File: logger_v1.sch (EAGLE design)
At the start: 141 parts, among them IC1 74HC595N, IC10 DS1307, IC12 LTC485N, IC2 7805T, IC4 REG1117, IC5 25LC080P, IC7 ATMEGA168-20P, IC9 LM358N, Q3 FQN1N50CI, Q4 32.768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

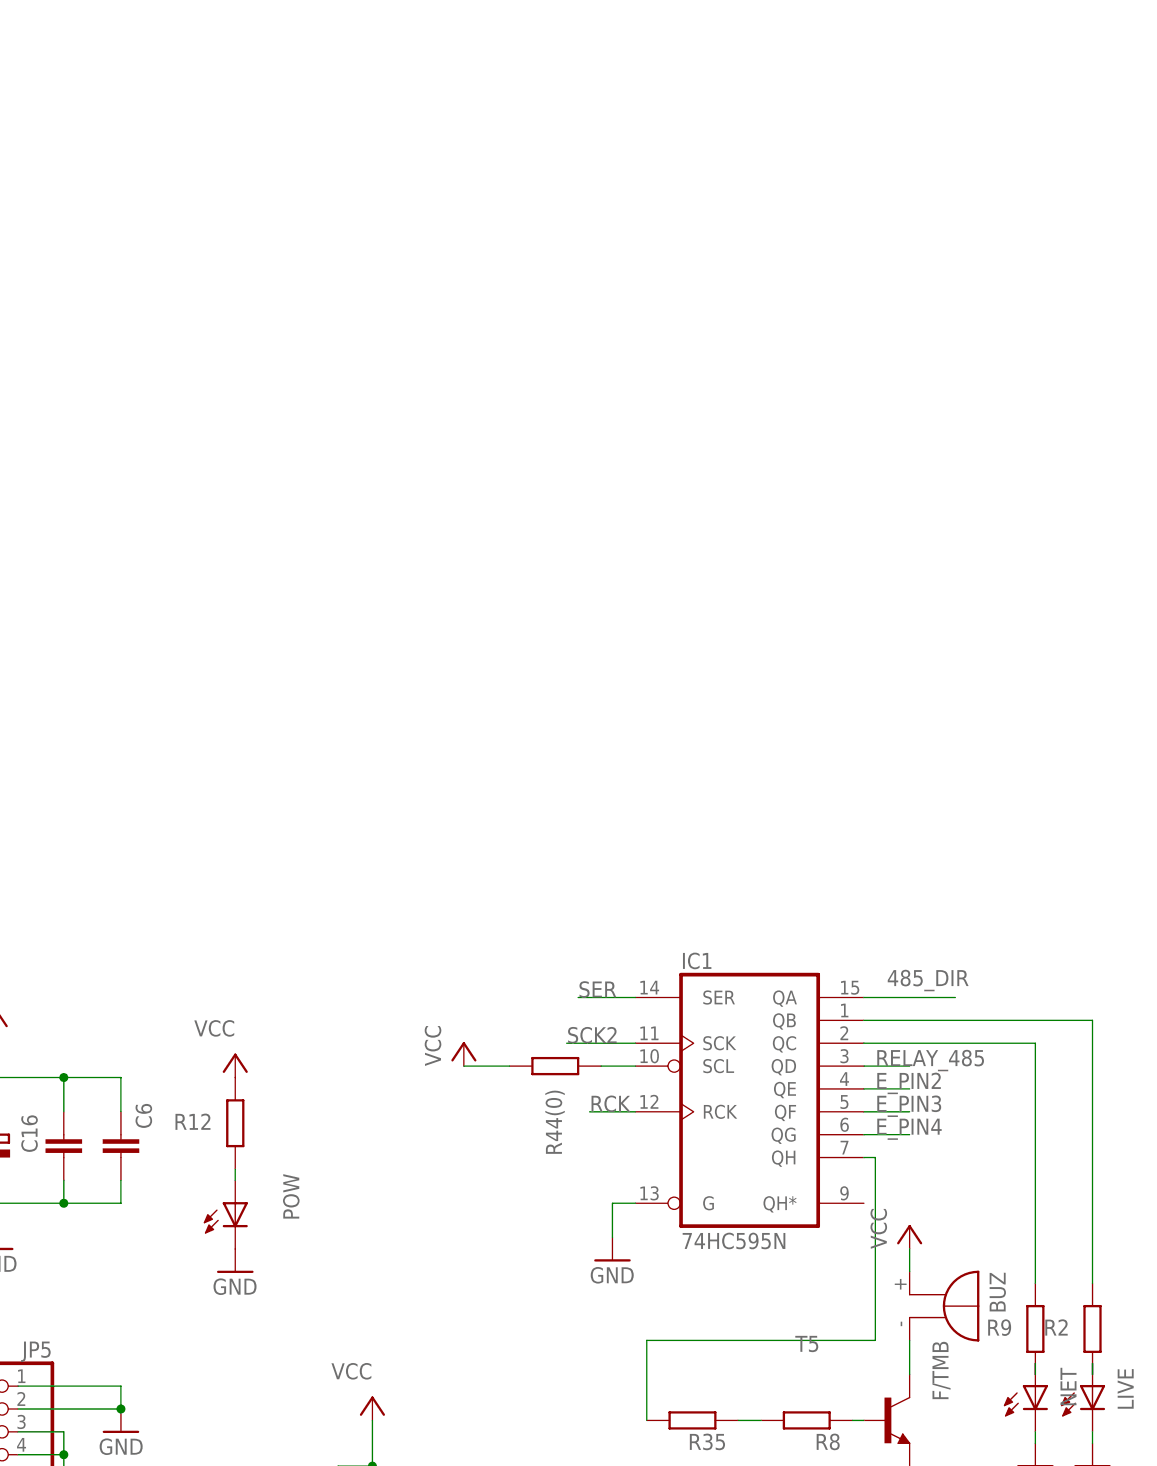
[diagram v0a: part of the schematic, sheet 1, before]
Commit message: led button ckt added
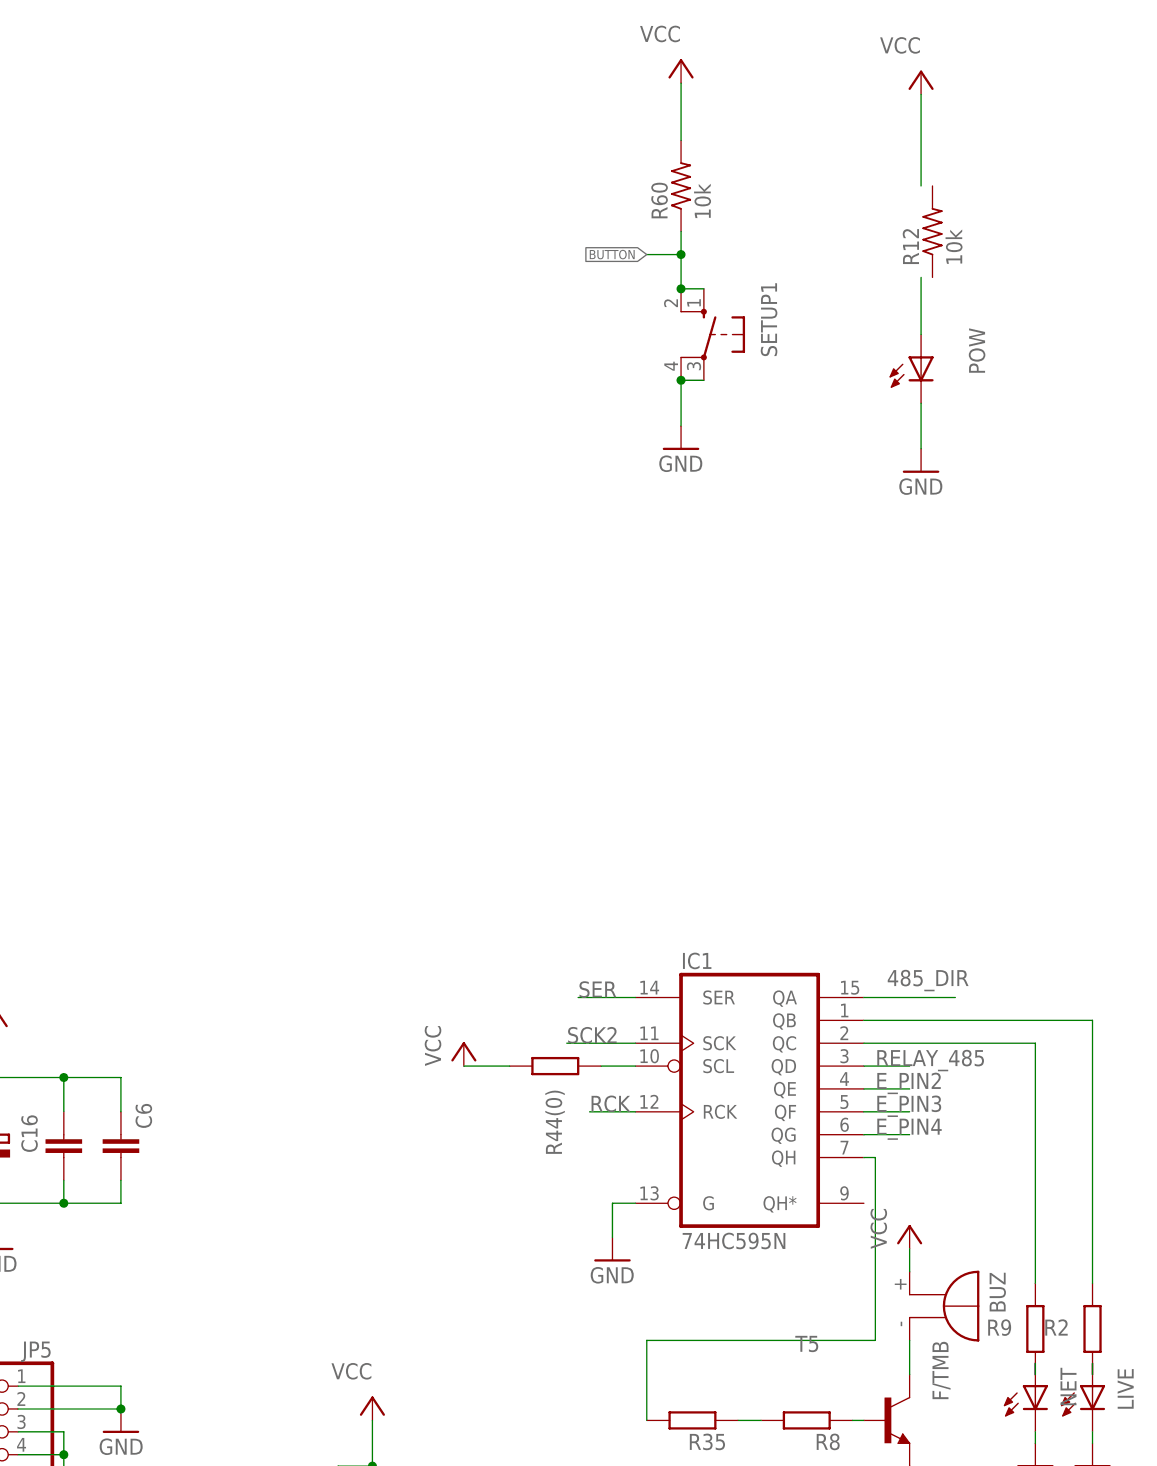
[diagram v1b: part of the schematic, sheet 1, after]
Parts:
- added R60: 10k, resistor:R-US_R0805
- added SETUP1: (no value), switch-omron:10-XX
- R12: value (none) -> 10k; device rcl:R-EU_0204/7 -> resistor:R-US_R0805
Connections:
- new net BUTTON: R60.1, SETUP1.S, SETUP1.S1
- net GND: now also SETUP1.P, SETUP1.P1
- net N$30: no longer R12.1
- net VCC: now also R60.2; no longer R12.2
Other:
- moved on the sheet: POW
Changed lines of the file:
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@@
 <setting verticaltext="up"/>
 </settings>
-<grid distance="0.05" unitdist="inch" unit="inch" style="lines" multiple="1" display="no" altdistance="0.01" altunitdist="inch" altunit="inch"/>
+<grid distance="0.1" unitdist="inch" unit="inch" style="lines" multiple="1" display="no" altdistance="0.01" altunitdist="inch" altunit="inch"/>
 <layers>
 <layer number="1" name="Top" color="4" fill="1" visible="no" active="no"/>
@@
 <layer number="59" name="tCarbon" color="7" fill="1" visible="no" active="no"/>
 <layer number="60" name="bCarbon" color="7" fill="1" visible="no" active="no"/>
+<layer number="88" name="SimResults" color="9" fill="1" visible="no" active="yes"/>
+<layer number="89" name="SimProbes" color="9" fill="1" visible="no" active="yes"/>
 <layer number="90" name="Modules" color="5" fill="1" visible="yes" active="yes"/>
 <layer number="91" name="Nets" color="2" fill="1" visible="yes" active="yes"/>
@@
 <layer number="112" name="tSilk" color="7" fill="1" visible="no" active="yes"/>
 <layer number="113" name="ReferenceLS" color="7" fill="1" visible="no" active="no"/>
+<layer number="114" name="Badge_Outline" color="7" fill="1" visible="no" active="no"/>
+<layer number="115" name="ReferenceISLANDS" color="7" fill="1" visible="no" active="no"/>
 <layer number="116" name="Patch_BOT" color="9" fill="4" visible="no" active="yes"/>
+<layer number="117" name="BACKMAAT1" color="7" fill="1" visible="yes" active="yes"/>
 <layer number="118" name="Rect_Pads" color="7" fill="1" visible="no" active="no"/>
+<layer number="119" name="KAP_TEKEN" color="7" fill="1" visible="yes" active="yes"/>
+<layer number="120" name="KAP_MAAT1" color="7" fill="1" visible="yes" active="yes"/>
 <layer number="121" name="_tsilk" color="7" fill="1" visible="no" active="yes"/>
 <layer number="122" name="_bsilk" color="7" fill="1" visible="no" active="yes"/>
@@
 <layer number="128" name="_bValues" color="7" fill="1" visible="no" active="yes"/>
 <layer number="129" name="Mask" color="7" fill="1" visible="yes" active="yes"/>
+<layer number="130" name="SMDSTROOK" color="7" fill="1" visible="yes" active="yes"/>
 <layer number="131" name="tAdjust" color="7" fill="1" visible="no" active="yes"/>
 <layer number="132" name="bAdjust" color="7" fill="1" visible="no" active="yes"/>
+<layer number="133" name="bottom_silk" color="7" fill="1" visible="yes" active="yes"/>
+<layer number="134" name="silk_top" color="7" fill="1" visible="yes" active="yes"/>
+<layer number="135" name="silk_bottom" color="7" fill="1" visible="yes" active="yes"/>
+<layer number="136" name="silktop" color="7" fill="1" visible="yes" active="yes"/>
+<layer number="137" name="silkbottom" color="7" fill="1" visible="yes" active="yes"/>
+<layer number="138" name="EEE" color="7" fill="1" visible="yes" active="yes"/>
+<layer number="139" name="_tKeepout" color="7" fill="1" visible="yes" active="yes"/>
+<layer number="141" name="ASSEMBLY_TOP" color="7" fill="1" visible="yes" active="yes"/>
+<layer number="143" name="PLACE_BOUND_TOP" color="7" fill="1" visible="yes" active="yes"/>
 <layer number="144" name="Drill_legend" color="7" fill="1" visible="no" active="yes"/>
+<layer number="145" name="DrillLegend_01-16" color="7" fill="1" visible="yes" active="yes"/>
+<layer number="146" name="DrillLegend_01-20" color="7" fill="1" visible="yes" active="yes"/>
+<layer number="147" name="PIN_NUMBER" color="7" fill="1" visible="yes" active="yes"/>
+<layer number="148" name="DrillLegend_01-20" color="7" fill="1" visible="yes" active="yes"/>
+<layer number="149" name="DrillLegend_02-15" color="7" fill="1" visible="yes" active="yes"/>
 <layer number="150" name="Notes" color="7" fill="1" visible="no" active="yes"/>
 <layer number="151" name="HeatSink" color="7" fill="1" visible="no" active="yes"/>
@@
 <layer number="154" name="FabDoc2" color="2" fill="1" visible="no" active="no"/>
 <layer number="155" name="FabDoc3" color="7" fill="15" visible="no" active="no"/>
+<layer number="166" name="AntennaArea" color="7" fill="1" visible="yes" active="yes"/>
+<layer number="168" name="4mmHeightArea" color="7" fill="1" visible="yes" active="yes"/>
 <layer number="199" name="Contour" color="7" fill="1" visible="no" active="yes"/>
 <layer number="200" name="200bmp" color="1" fill="10" visible="no" active="yes"/>
@@
 <part name="P+3" library="supply1" deviceset="VCC" device=""/>
 <part name="POW" library="led" deviceset="LED" device="3MM"/>
-<part name="R12" library="rcl" deviceset="R-EU_" device="0204/7"/>
 <part name="P+4" library="supply1" deviceset="+12V" device=""/>
 <part name="C13" library="rcl" deviceset="CPOL-EU" device="TT2D6"/>
@@
 <part name="GND36" library="supply1" deviceset="GND" device=""/>
 <part name="R59" library="rcl" deviceset="R-EU_" device="0204/7"/>
+<part name="GND16" library="supply1" deviceset="GND" device=""/>
+<part name="R60" library="resistor" deviceset="R-US_" device="R0805" value="10k"/>
+<part name="P+14" library="supply1" deviceset="VCC" device=""/>
+<part name="SETUP1" library="switch-omron" deviceset="10-XX" device=""/>
+<part name="R12" library="resistor" deviceset="R-US_" device="R0805" value="10k"/>
 </parts>
 <sheets>
@@
 <instance part="P+8" gate="1" x="168.91" y="-8.89"/>
 <instance part="GND7" gate="1" x="170.18" y="0" rot="MR0"/>
-<instance part="POW" gate="G$1" x="182.88" y="25.4" smashed="yes">
-<attribute name="NAME" x="188.214" y="28.702" size="1.778" layer="95" rot="R270"/>
-<attribute name="VALUE" x="188.595" y="20.828" size="1.778" layer="96" rot="R90"/>
-</instance>
-<instance part="R12" gate="G$1" x="182.88" y="34.29" smashed="yes" rot="R90">
-<attribute name="NAME" x="180.34" y="35.3314" size="1.778" layer="95" rot="R180"/>
-<attribute name="VALUE" x="186.182" y="30.48" size="1.778" layer="96" rot="R90"/>
-</instance>
-<instance part="GND34" gate="1" x="182.88" y="17.78" smashed="yes">
-<attribute name="VALUE" x="180.34" y="15.24" size="1.778" layer="96"/>
-</instance>
-<instance part="P+25" gate="VCC" x="182.88" y="41.91" smashed="yes">
-<attribute name="VALUE" x="182.88" y="45.72" size="1.778" layer="96" rot="R180"/>
+<instance part="POW" gate="G$1" x="259.08" y="119.38" smashed="yes">
+<attribute name="NAME" x="264.414" y="122.682" size="1.778" layer="95" rot="R270"/>
+<attribute name="VALUE" x="264.795" y="114.808" size="1.778" layer="96" rot="R90"/>
+</instance>
+<instance part="GND34" gate="1" x="259.08" y="106.68" smashed="yes">
+<attribute name="VALUE" x="256.54" y="104.14" size="1.778" layer="96"/>
+</instance>
+<instance part="P+25" gate="VCC" x="259.08" y="151.13" smashed="yes">
+<attribute name="VALUE" x="259.08" y="154.94" size="1.778" layer="96" rot="R180"/>
 </instance>
 <instance part="JP2" gate="A" x="19.05" y="118.11"/>
@@
 <attribute name="VALUE" x="168.656" y="35.179" size="1.778" layer="96" rot="R180"/>
 </instance>
+<instance part="GND16" gate="1" x="232.41" y="109.22" smashed="yes">
+<attribute name="VALUE" x="229.87" y="106.68" size="1.778" layer="96"/>
+</instance>
+<instance part="R60" gate="G$1" x="232.41" y="138.43" rot="R90"/>
+<instance part="P+14" gate="VCC" x="232.41" y="152.4" smashed="yes">
+<attribute name="VALUE" x="232.41" y="156.21" size="1.778" layer="96" rot="R180"/>
+</instance>
+<instance part="SETUP1" gate="1" x="234.95" y="121.92" smashed="yes" rot="MR0">
+<attribute name="NAME" x="241.3" y="119.38" size="1.778" layer="95" rot="MR90"/>
+<attribute name="VALUE" x="238.76" y="125.095" size="1.778" layer="96" rot="MR90"/>
+</instance>
+<instance part="R12" gate="G$1" x="260.35" y="133.35" rot="R90"/>
 </instances>
 <busses>
@@
 <pinref part="POW" gate="G$1" pin="C"/>
 <pinref part="GND34" gate="1" pin="GND"/>
+<wire x1="259.08" y1="109.22" x2="259.08" y2="114.3" width="0.1524" layer="91"/>
 </segment>
 <segment>
@@
 <pinref part="GND36" gate="1" pin="GND"/>
 <wire x1="349.25" y1="-58.42" x2="349.25" y2="-59.69" width="0.1524" layer="91"/>
+</segment>
+<segment>
+<pinref part="GND16" gate="1" pin="GND"/>
+<wire x1="232.41" y1="111.76" x2="232.41" y2="116.84" width="0.1524" layer="91"/>
+<pinref part="SETUP1" gate="1" pin="P1"/>
+<pinref part="SETUP1" gate="1" pin="P"/>
+<wire x1="234.95" y1="116.84" x2="232.41" y2="116.84" width="0.1524" layer="91"/>
+<junction x="232.41" y="116.84"/>
 </segment>
 </net>
@@
 </segment>
 <segment>
-<pinref part="R12" gate="G$1" pin="2"/>
 <pinref part="P+25" gate="VCC" pin="VCC"/>
+<wire x1="259.08" y1="148.59" x2="259.08" y2="138.43" width="0.1524" layer="91"/>
 </segment>
 <segment>
@@
 <pinref part="R48(0)" gate="G$1" pin="2"/>
 <pinref part="P+7" gate="VCC" pin="VCC"/>
+</segment>
+<segment>
+<pinref part="R60" gate="G$1" pin="2"/>
+<pinref part="P+14" gate="VCC" pin="VCC"/>
+<wire x1="232.41" y1="149.86" x2="232.41" y2="143.51" width="0.1524" layer="91"/>
 </segment>
 </net>
@@
 <segment>
 <pinref part="POW" gate="G$1" pin="A"/>
-<pinref part="R12" gate="G$1" pin="1"/>
-<wire x1="182.88" y1="29.21" x2="182.88" y2="27.94" width="0.1524" layer="91"/>
+<wire x1="259.08" y1="128.27" x2="259.08" y2="121.92" width="0.1524" layer="91"/>
 </segment>
 </net>
@@
 </segment>
 </net>
+<net name="BUTTON" class="0">
+<segment>
+<pinref part="R60" gate="G$1" pin="1"/>
+<wire x1="232.41" y1="133.35" x2="232.41" y2="130.81" width="0.1524" layer="91"/>
+<wire x1="232.41" y1="130.81" x2="232.41" y2="127" width="0.1524" layer="91"/>
+<wire x1="232.41" y1="130.81" x2="228.6" y2="130.81" width="0.1524" layer="91"/>
+<junction x="232.41" y="130.81"/>
+<label x="228.6" y="130.81" size="1.016" layer="95" rot="R180" xref="yes"/>
+<pinref part="SETUP1" gate="1" pin="S1"/>
+<pinref part="SETUP1" gate="1" pin="S"/>
+<wire x1="234.95" y1="127" x2="232.41" y2="127" width="0.1524" layer="91"/>
+<junction x="232.41" y="127"/>
+</segment>
+</net>
